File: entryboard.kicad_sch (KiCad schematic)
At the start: 23 parts, among them J1 Conn_01x01, J10 Conn_01x01, J11 Conn_01x01, J12 Conn_01x01, J13 Conn_01x03_Pin, J14 USB_C_Receptacle, J2 Conn_01x01, J3 Conn_01x01, J4 Conn_01x01, J5 Conn_01x01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

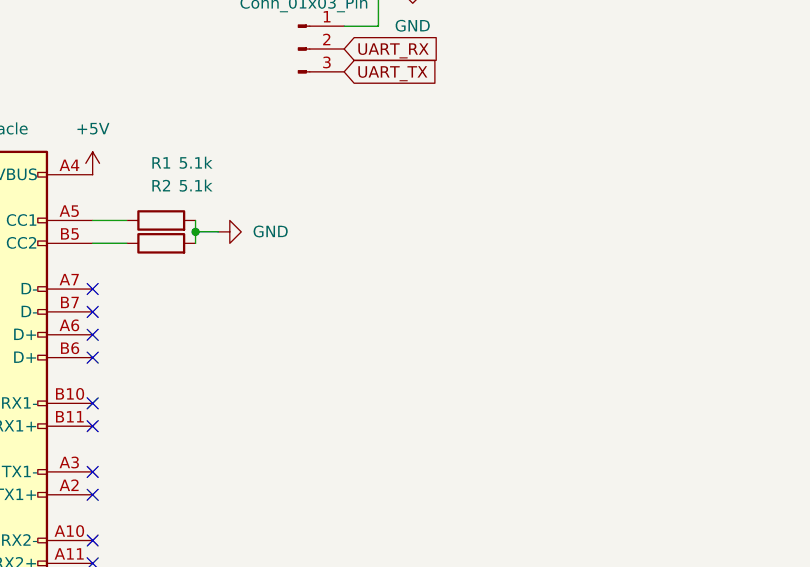
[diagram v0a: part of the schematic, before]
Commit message: feat: add headers for keys, and another ground point
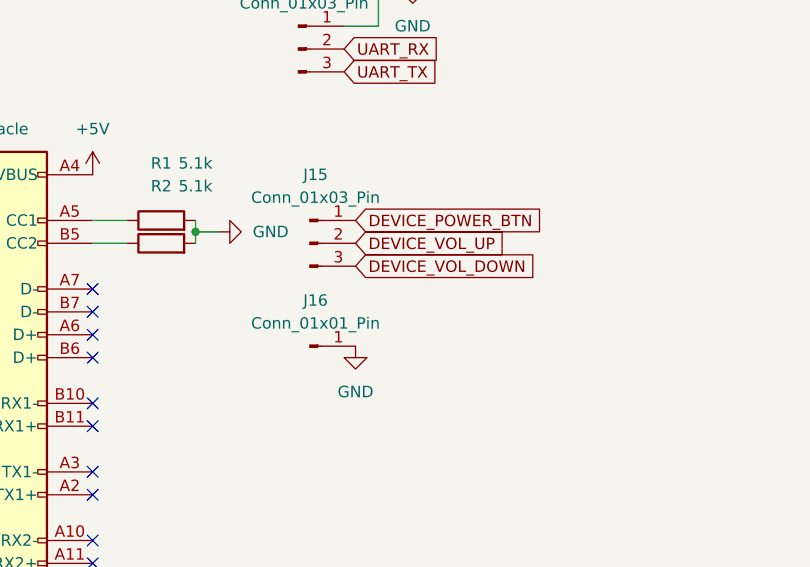
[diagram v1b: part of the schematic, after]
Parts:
- added J15: Conn_01x03_Pin, Connector_PinHeader_1.00mm:PinHeader_1x03_P1.00mm_Vertical, symbol Connector:Conn_01x03_Pin
- added J16: Conn_01x01_Pin, Connector_PinHeader_1.00mm:PinHeader_1x01_P1.00mm_Vertical, symbol Connector:Conn_01x01_Pin
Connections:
- net DEVICE_POWER_BTN: now also J15.1 (Pin_1)
- net DEVICE_VOL_DOWN: now also J15.3 (Pin_3)
- net DEVICE_VOL_UP: now also J15.2 (Pin_2)
- net GND: now also J16.1 (Pin_1)

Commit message: fix: Use 2.54mm pitch header pins
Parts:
- J13, J15: footprint Connector_PinHeader_1.00mm:PinHeader_1x03_P1.00mm_Vertical -> Connector_PinHeader_2.54mm:PinHeader_1x03_P2.54mm_Vertical
- J9: footprint Connector_PinHeader_1.00mm:PinHeader_1x02_P1.00mm_Vertical -> Connector_PinHeader_2.54mm:PinHeader_1x02_P2.54mm_Vertical
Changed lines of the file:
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@@
 			)
 		)
-		(property "Footprint" "Connector_PinHeader_1.00mm:PinHeader_1x03_P1.00mm_Vertical"
+		(property "Footprint" "Connector_PinHeader_2.54mm:PinHeader_1x03_P2.54mm_Vertical"
 			(at 71.12 97.79 0)
 			(effects
@@
 			)
 		)
-		(property "Footprint" "Connector_PinHeader_1.00mm:PinHeader_1x03_P1.00mm_Vertical"
+		(property "Footprint" "Connector_PinHeader_2.54mm:PinHeader_1x03_P2.54mm_Vertical"
 			(at 69.85 76.2 0)
 			(effects
@@
 			)
 		)
-		(property "Footprint" "Connector_PinHeader_1.00mm:PinHeader_1x02_P1.00mm_Vertical"
+		(property "Footprint" "Connector_PinHeader_2.54mm:PinHeader_1x02_P2.54mm_Vertical"
 			(at 69.85 40.64 0)
 			(effects

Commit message: too much to say
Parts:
- removed J8: USB_A, Connector_USB:USB_A_Kycon_KUSBX-AS1N-B_Horizontal, symbol Connector:USB_A
- added J8: Conn_01x01_Pin, Connector_PinHeader_1.00mm:PinHeader_1x01_P2.54mm_Vertical, symbol Connector:Conn_01x01_Pin
- added R3, R4: 3.3k, Resistor_SMD:R_1206_3216Metric_Pad1.30x1.75mm_HandSolder, symbol Device:R
- J1, J10, J11, J12, J2, J3, J4, J5: footprint TestPoint:TestPoint_Pad_1.0x1.0mm -> Connector_PinSocket_2.54mm:PinSocket_1x01_P2.54mm_Vertical
- J16: footprint Connector_PinHeader_1.00mm:PinHeader_1x01_P1.00mm_Vertical -> Connector_PinHeader_2.54mm:PinHeader_1x01_P2.54mm_Vertical
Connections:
- net +5V: now also J8.1 (Pin_1)
- net DEVICE_USB+: now also J9.1 (Pin_1)
- net DEVICE_USB_ID: no longer J9.1 (Pin_1)
- net GND: now also R4.1
- net UART_RX: now also R3.2, R4.2; no longer J7.1 (Pin_1)
- new net: J7.1 (Pin_1), R3.1
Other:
- moved on the sheet: J11, J13, J14, J15, J16, J6, J7, J9, R1, R2

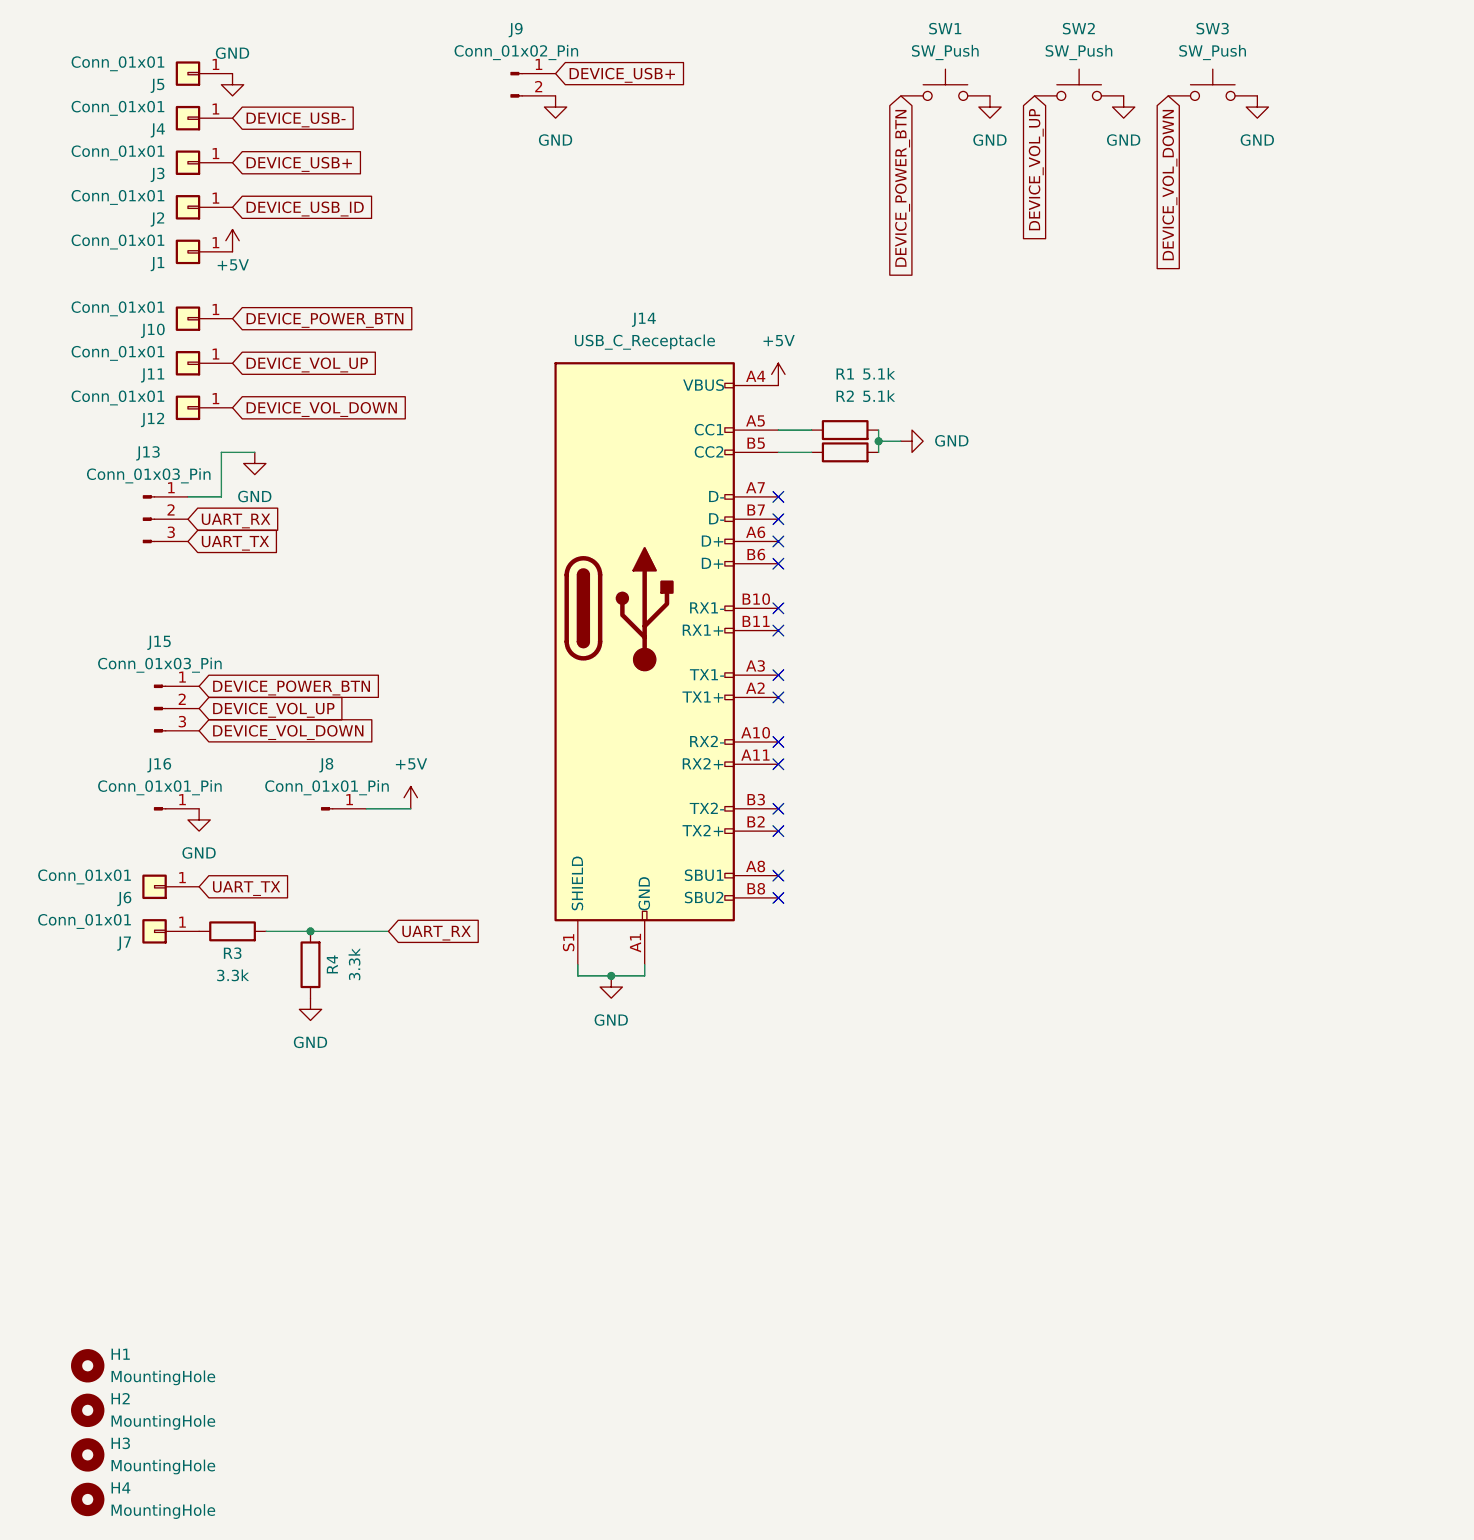
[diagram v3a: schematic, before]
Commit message: refactor: drop usbs, smaller board
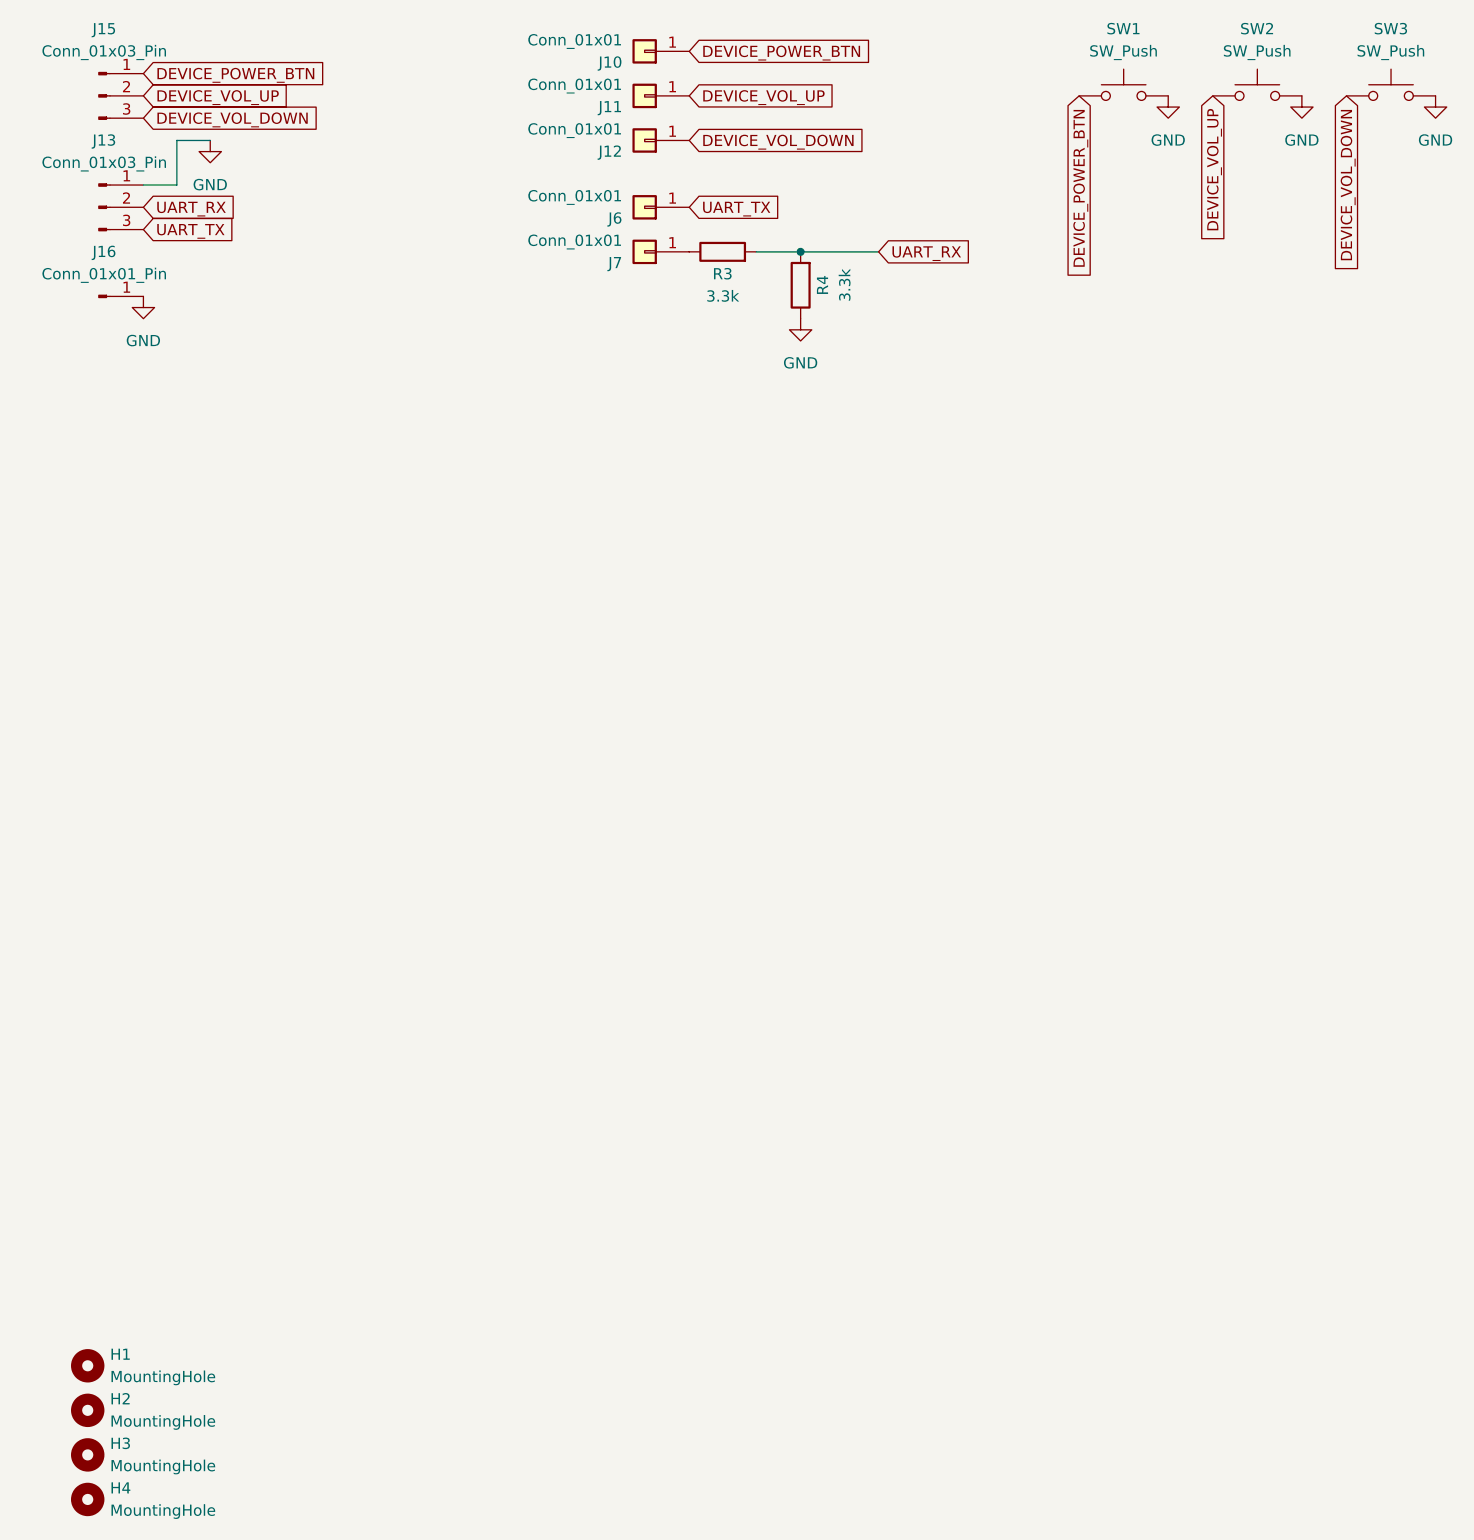
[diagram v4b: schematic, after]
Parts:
- removed J1, J2, J3, J4, J5: Conn_01x01, Connector_PinSocket_2.54mm:PinSocket_1x01_P2.54mm_Vertical, symbol Connector_Generic:Conn_01x01
- removed J14: USB_C_Receptacle, Connector_USB:USB_C_Receptacle_GCT_USB4105-xx-A_16P_TopMnt_Horizontal, symbol Connector:USB_C_Receptacle
- removed J8: Conn_01x01_Pin, Connector_PinHeader_1.00mm:PinHeader_1x01_P2.54mm_Vertical, symbol Connector:Conn_01x01_Pin
- removed J9: Conn_01x02_Pin, Connector_PinHeader_2.54mm:PinHeader_1x02_P2.54mm_Vertical, symbol Connector:Conn_01x02_Pin
- removed R1, R2: 5.1k, Resistor_SMD:R_1206_3216Metric_Pad1.30x1.75mm_HandSolder, symbol Device:R
- SW1, SW2, SW3: footprint Button_Switch_THT:SW_PUSH-12mm -> Button_Switch_THT:SW_PUSH_6mm
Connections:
- no-connect marks 14 -> 0
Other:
- title: (none) -> entryboard
- moved on the sheet: J10, J11, J12, J13, J15, J16, J6, J7, R3, R4, SW1
